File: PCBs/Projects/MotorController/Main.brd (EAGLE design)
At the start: 172.7 x 99.1 mm, 122 parts, among them Q1 ZXMP10A17GQ, Q2 MMBT5551LT1G, Q3 BUK9240-100A.118, Q4 BUK9240-100A.118, U1 DRV8301, U11 LT4356-2, U2 ESDA6V1SC6Y, U3 ESDA6V1SC6Y, U4 ESDA6V1SC6Y, U5 TMP101, U6 ACS758LCB, U7 ESDA6V1SC6Y, U8 MTI85W100GC

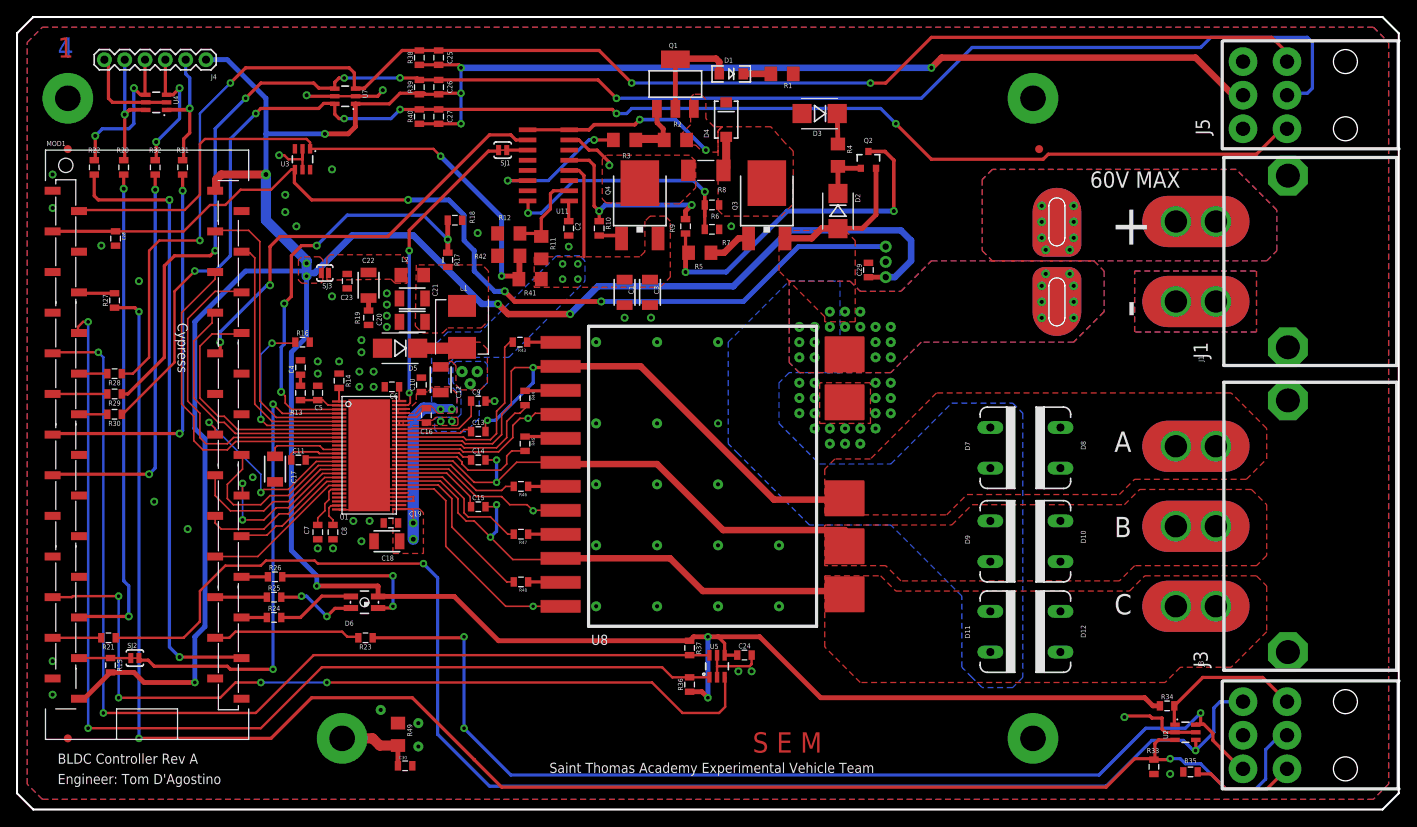
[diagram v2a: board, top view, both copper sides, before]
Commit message: Footprint updates and drc fixes -Additionally, filter cap added to throttle
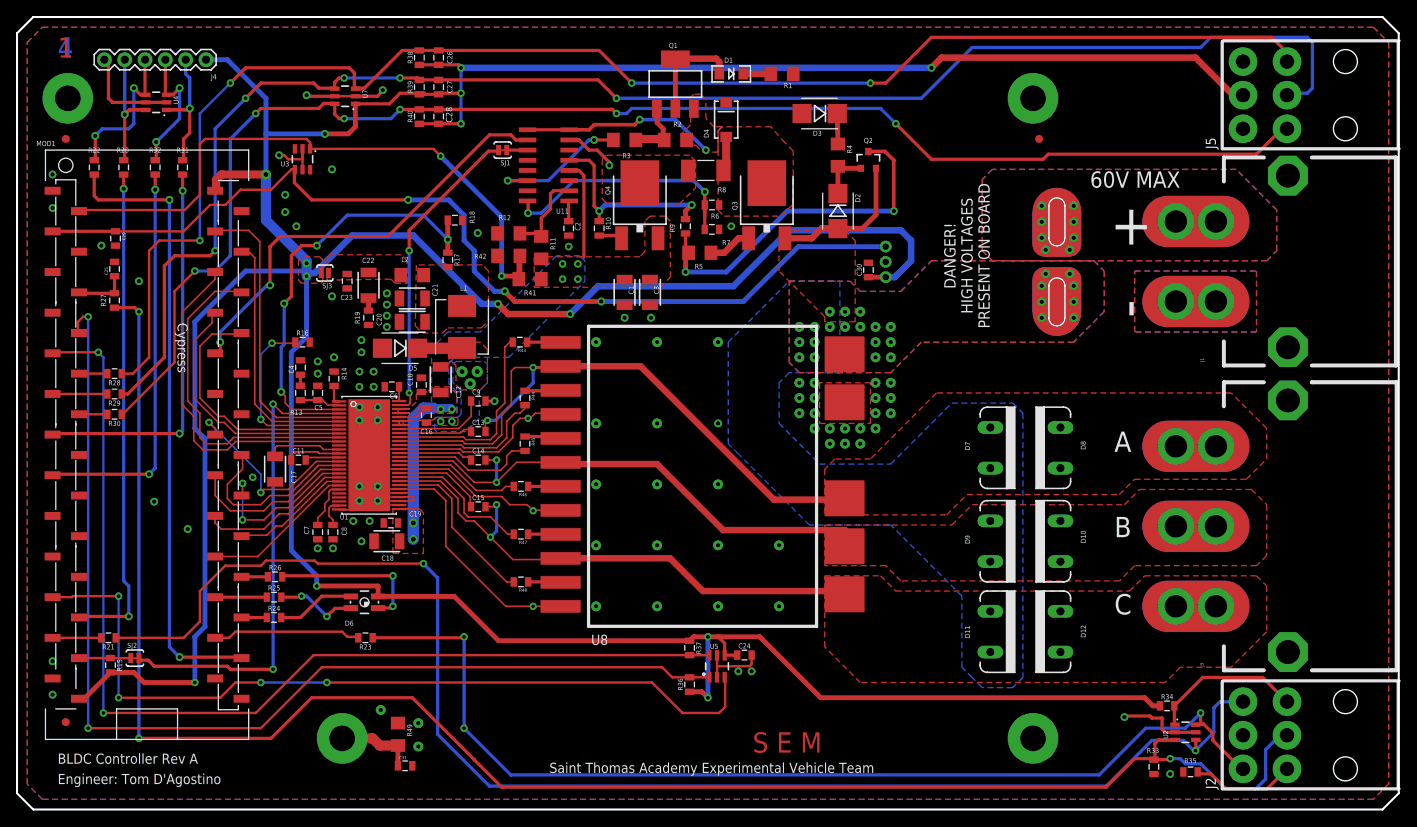
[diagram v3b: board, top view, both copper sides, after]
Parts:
- added C31: 0.01u, SparkFun-Capacitors:0805
- C25: value 10n -> 0.1u
- C29: value 0.1u -> 10n
- C30: value 0.01u -> 0.1u
- moved C29 94.2 mm to (12.3, 68.8), turned to 270 degrees
- moved C30 84.8 mm to (106.4, 64.9), turned to 90 degrees
- moved C25 48.4 mm to (12.2, 65.0)
- moved C28 43.2 mm to (52.7, 84.1), turned to 90 degrees
- moved C27 3.68 mm to (52.7, 87.8)
- moved C26 3.68 mm to (52.7, 91.4)
- moved FD3 2.05 mm to (6.10, 8.38)
- moved FD2 1.30 mm to (6.10, 81.3)
- moved FD1 1.27 mm to (127.8, 81.3)
- moved R14 0.68 mm to (39.6, 51.3)
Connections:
- net 5V: now also C28.1, C30.1; no longer C25.1, C29.1
- net GND: now also C25.2, C31.2; no longer C28.2
- net H1: now also C26.2; no longer C25.2
- net H2: now also C27.2; no longer C26.2
- net H3: now also C28.2; no longer C27.2
- net ISENSE: now also C29.1; no longer C28.1
- net N$31: now also C31.1; no longer C30.1
- net N$39: now also C25.1
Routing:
- net N$39: track 4.49 -> 6.63 mm
- net SCL: track 134.5 -> 135.8 mm
- net N$2: track 1.71 -> 2.58 mm
- net GND: track 176.3 -> 176.5 mm, vias 88 -> 96
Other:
- board text added: "DANGER\! HIGH VOLTAGES PRESENT ON BOARD"
- board text removed: "J1"
- board text removed: "J3"
- board text removed: "J5"

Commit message: RevA board sent to board house -lots of little silkscreen additions -tmp101 datasheet added -CAM files saved
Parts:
- added FRAME1, FRAME2, FRAME3, FRAME4, FRAME5, FRAME6: FRAME-LEDGER, SparkFun-Aesthetics:CREATIVE_COMMONS
- moved C24 9.54 mm to (81.5, 18.4), turned to 180 degrees
- moved R36 6.86 mm to (90.9, 13.0)
- moved R37 6.13 mm to (88.0, 13.0), turned to 90 degrees
- moved U5 2.98 mm to (85.6, 17.7), turned to 90 degrees
- moved C7 1.27 mm to (37.6, 33.4)
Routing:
- net SCL: track 135.8 -> 146.9 mm, vias 2 -> 4
- net GND: track 176.5 -> 168.1 mm, vias 96 -> 95
- net T_ALERT: track 103.2 -> 111.4 mm, vias 4 -> 6
- net SDA: track 129.9 -> 137.5 mm, vias 2 -> 4
- net 5V: track 533.6 -> 529.1 mm, vias 14 -> 12
- net N$5: track 6.15 -> 4.88 mm
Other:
- board text added: ""Don't forget the heatshrink!""
- board text added: "5v"
- board text added: "D"
- board text added: "DO"
- board text added: "Fabrication Notes: 1: The milling layer denotes internal cutouts. 2: Internal cutouts are not plated."
- board text added: "GND"
- board text added: "H1"
- board text added: "H2"
- board text added: "H3"
- board text added: "IO"
- board text added: "R"
- board text added: "RX"
- board text added: "T1"
- board text added: "T2"
- board text added: "T3"
- board text added: "TX"

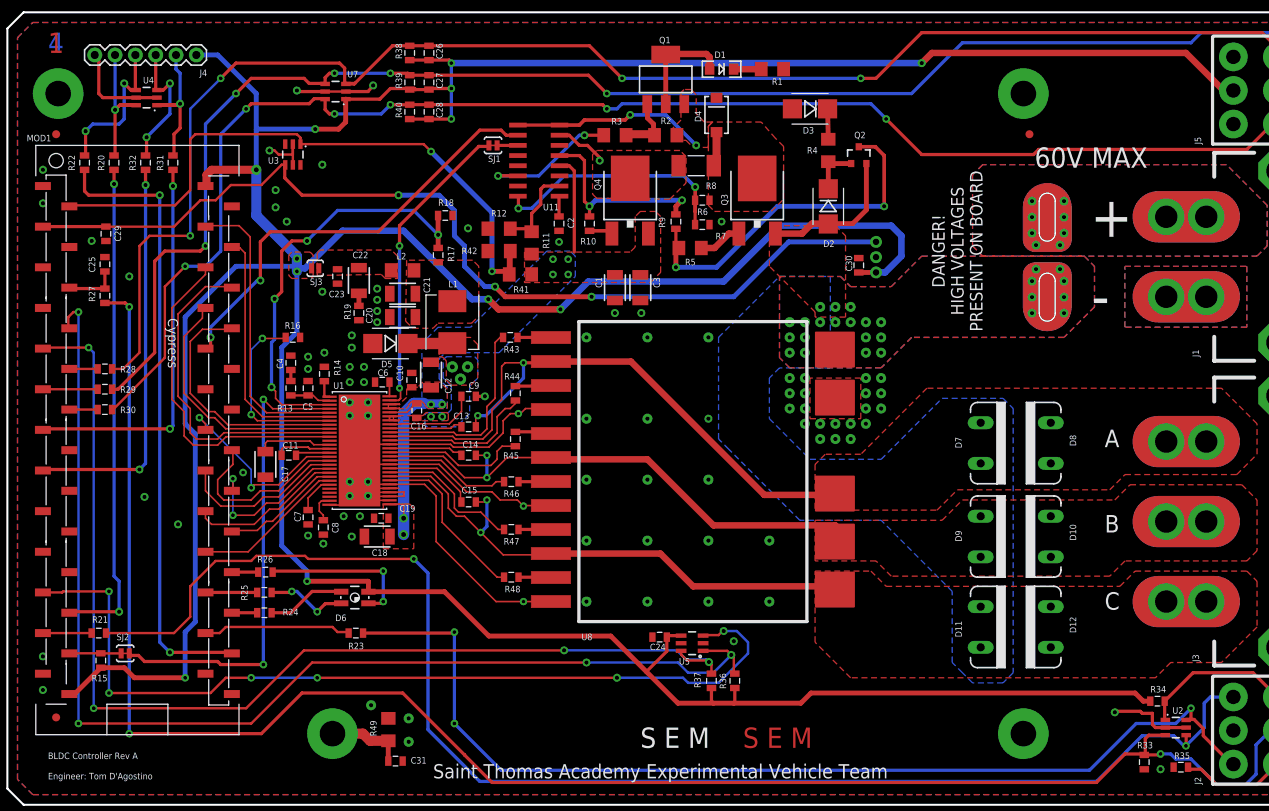
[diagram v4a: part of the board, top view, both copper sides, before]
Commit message: Added pdfs of RevB schematic and pcb -Cleaned schematic of RevB
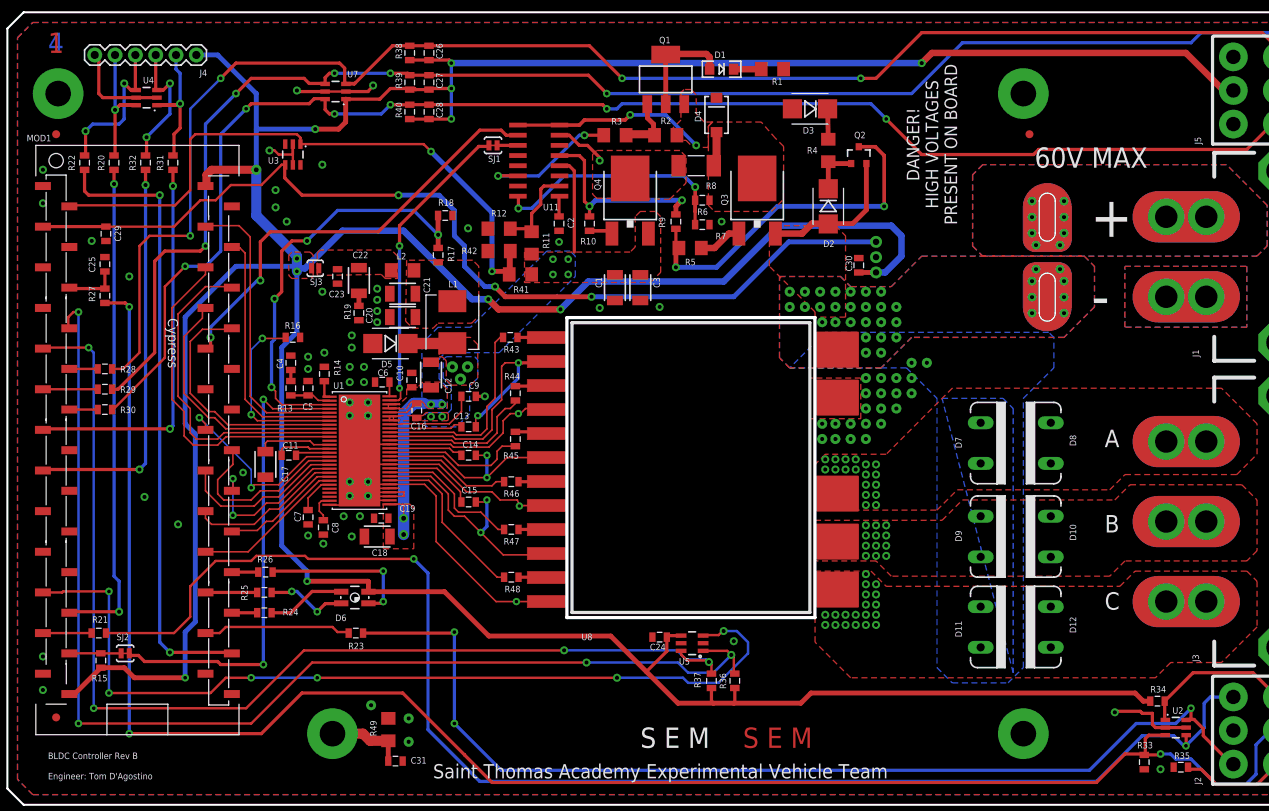
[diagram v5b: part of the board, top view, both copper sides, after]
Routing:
- net A: track 82.2 -> 39.1 mm, vias 2 -> 20
- net B: track 71.3 -> 28.7 mm, vias 2 -> 14
- net C: track 68.5 -> 31.5 mm, vias 2 -> 21
- net GND: track 168.1 -> 168.0 mm, vias 95 -> 80
- net V_BATT: vias 18 -> 26
- added copper zone on layer 15, net KEEPOUT
- added copper zone on layer 2, net KEEPOUT
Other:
- board text added: "BLDC Controller Rev B"
- board text removed: "BLDC Controller Rev A"

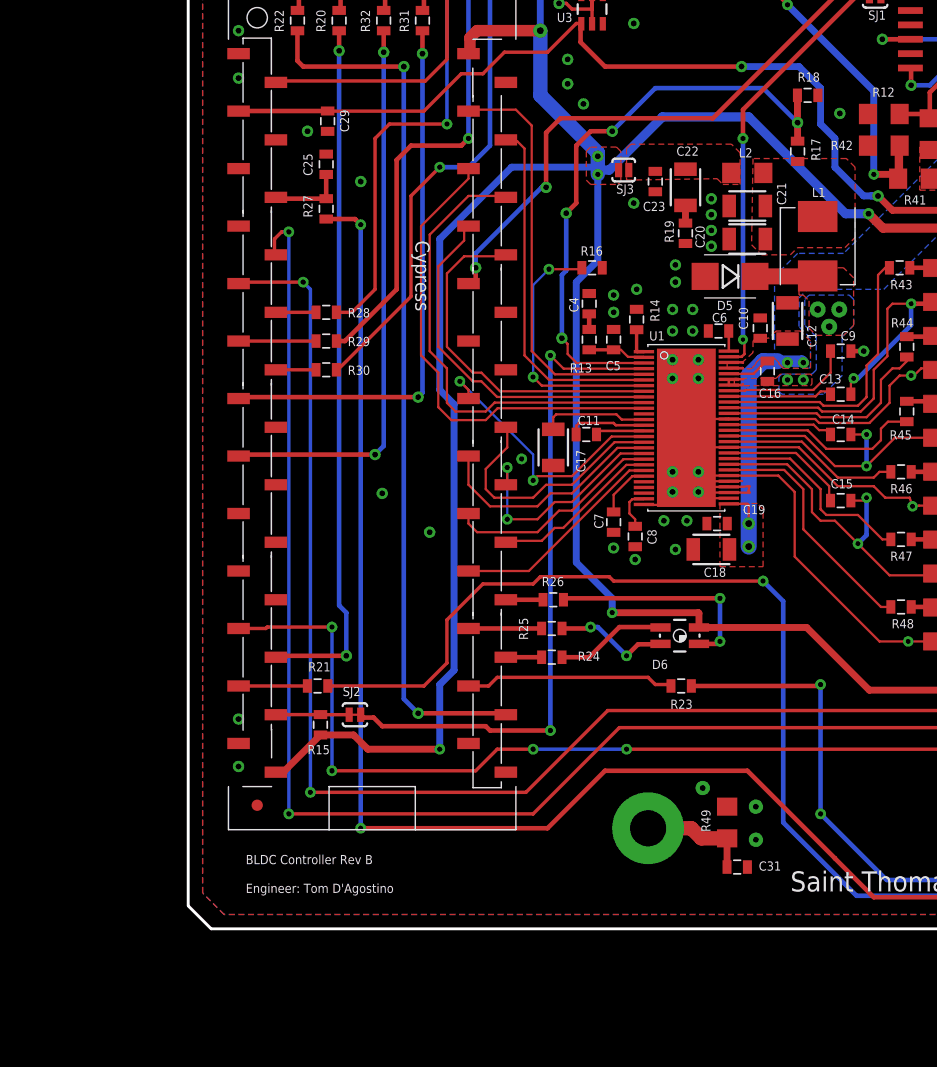
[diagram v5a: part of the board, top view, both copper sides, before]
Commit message: Starting work on Rev C, Rev B has been abandoned but not forgotten -Adding datasheets of some the the parts rec C will utilize -Added some power supply calculations -Added LT3045 and LT8631 parts in the IC library
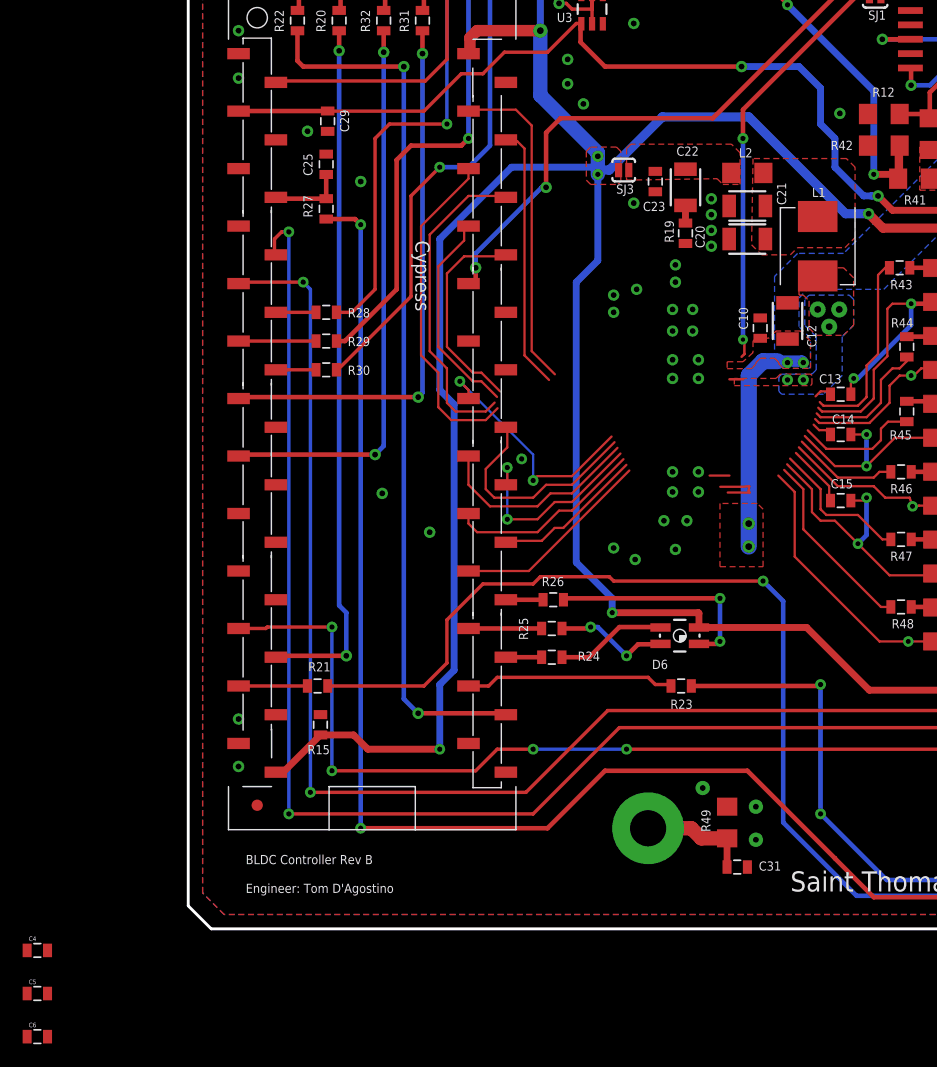
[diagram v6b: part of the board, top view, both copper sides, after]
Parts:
- removed C11, C9: 22n, SparkFun-Capacitors:0805
- removed C16, C19: 0.1u, SparkFun-Capacitors:0805
- removed C17: 2.2u, SparkFun-Capacitors:1210
- removed C18: 4.7u, SparkFun-Capacitors:1210
- removed C7, C8: 1u, SparkFun-Capacitors:0805
- removed D5: PMEG10030ELPX, SparkFun-DiscreteSemi:SMB-DIODE
- removed R13: 16.2K, SparkFun-Resistors:0805
- removed R14: 250k, SparkFun-Resistors:0805
- removed R16: 100, SparkFun-Resistors:0805
- removed R17: 51k, SparkFun-Resistors:0805
- removed R18: 10k, SparkFun-Resistors:0805
- removed SJ2: SOLDERJUMPERTRACE, SparkFun-Retired:SJ_2S-TRACE
- removed U1: DRV8301, IC:HTSSOP_56
- added FRAME8: FRAME-LEDGER, SparkFun-Aesthetics:CREATIVE_COMMONS
- C4: value 6.8N -> 0.1u
- C5: value 120P -> 0.1u
- C6: value 22n -> 0.1u
- moved C6 86.7 mm to (-13.3, -12.1), turned to 0 degrees
- moved C5 77.0 mm to (-13.3, -8.26), turned to 0 degrees
- moved C4 75.1 mm to (-13.3, -4.45), turned to 0 degrees
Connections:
- removed net 3.3V: C9.1, U1.49
- removed net IND_LOOP_IN: C16.2, D5.C, L1.P$1, U1.50, U1.51
- removed net N$10: C8.1, U1.27
- removed net N$12: C6.1, U1.56
- removed net N$14: R17.1, R18.2, U1.3
- removed net N$15: C16.1, U1.52
- removed net N$17: C11.2, U1.15
- removed net N$18: C11.1, U1.14
- removed net N$21: C17.1, U1.13
- removed net N$26: R16.1, U1.7
- removed net N$45: SJ2.2, U1.4
- removed net N$6: C5.1, R13.1, U1.2
- net !CS: no longer U1.8
- net !FAULT: no longer U1.6
- net !OCTW: no longer U1.5
- net A: now also C6.2; no longer U1.46
- net B: now also C5.2; no longer U1.41
- net BUCK-EN: no longer U1.55
- net C: now also C4.2; no longer U1.36
- net EN_GATE: no longer U1.16
- net GH_A: no longer U1.47
- net GH_B: no longer U1.42
- net GH_C: no longer U1.37
- net GL_A: no longer U1.45
- net GL_B: no longer U1.40
- net GL_C: no longer U1.35
- net GND: no longer C17.2, C18.1, C19.2, C4.2, C5.2, C6.2, C7.2, C8.2, C9.2, D5.A, R14.1, R16.2, R18.1, U1.28, U1.30, U1.31, U1.32, U1.33, U1.34, U1.39, U1.44, U1.EXP
- net IND_LOOP_OUT: no longer L1.P$2, R17.2
- net INH_A: no longer U1.17
- net INH_B: no longer U1.19
- net INH_C: no longer U1.21
- net INL_A: no longer U1.18
- net INL_B: no longer U1.20
- net INL_C: no longer U1.22
- net MISO: no longer U1.10
- net MOSI: no longer U1.9
- net N$2: now also C6.1; no longer R14.2, U1.1
- net N$24: no longer U1.48
- net N$25: no longer U1.38
- net N$3: no longer R13.2
- net N$30: no longer U1.43
- net N$5: now also C5.1; no longer C7.1, U1.23
- net PWRGD: no longer R15.1, SJ2.1
- net SCLK: no longer U1.11
- net VCC: no longer C18.2, C19.1, U1.29, U1.53, U1.54
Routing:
- net GND: track 168.0 -> 104.1 mm, vias 80 -> 79
- net N$45: track 59.2 -> 0.00 mm, vias 2 -> 0
- net N$14: track 53.2 -> 0.00 mm, vias 4 -> 0
- net N$26: track 23.2 -> 0.00 mm, vias 2 -> 0
- net MISO: track 41.7 -> 28.5 mm
- net MOSI: track 31.8 -> 18.8 mm
- net SCLK: track 42.5 -> 29.6 mm
- net !CS: track 31.4 -> 18.7 mm
- net 3.3V: track 11.6 -> 0.00 mm
- net N$21: track 9.37 -> 0.00 mm
- net !FAULT: track 32.0 -> 23.6 mm
- net GH_A: track 25.1 -> 17.1 mm
- net A: track 39.1 -> 31.2 mm
- net !OCTW: track 36.9 -> 29.1 mm
- net GL_A: track 19.5 -> 11.7 mm
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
